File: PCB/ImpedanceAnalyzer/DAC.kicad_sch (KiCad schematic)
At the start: 88 parts, among them U14 OPA4830, U17 OPA4830, U6 LTC1668CG

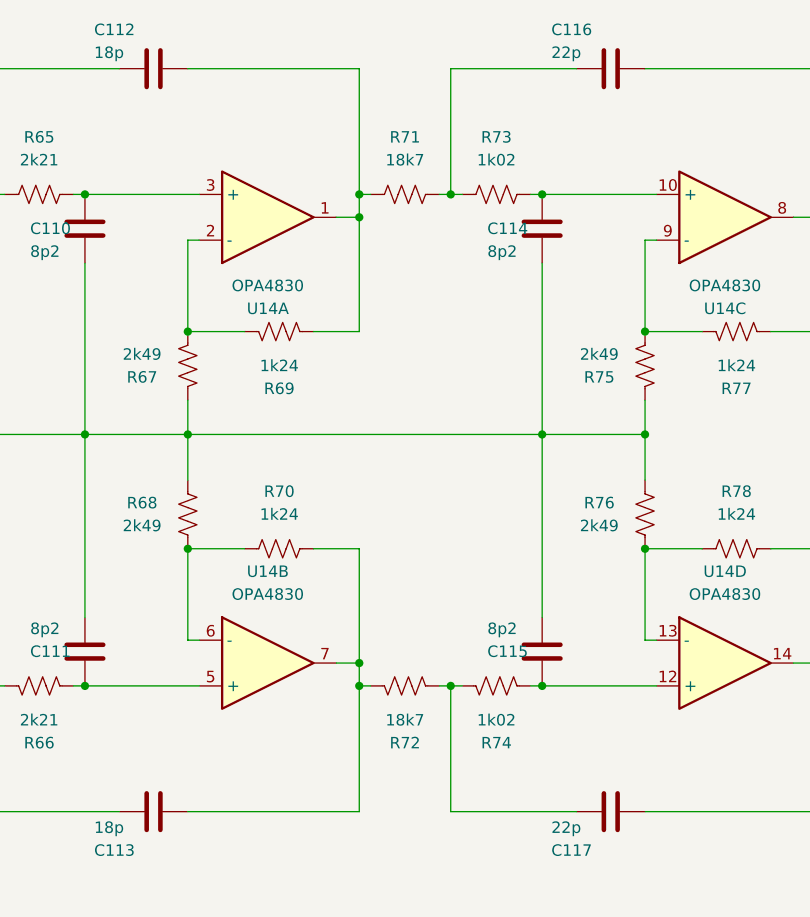
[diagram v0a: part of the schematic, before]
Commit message: STM32 SimpleSample code with PGA and range
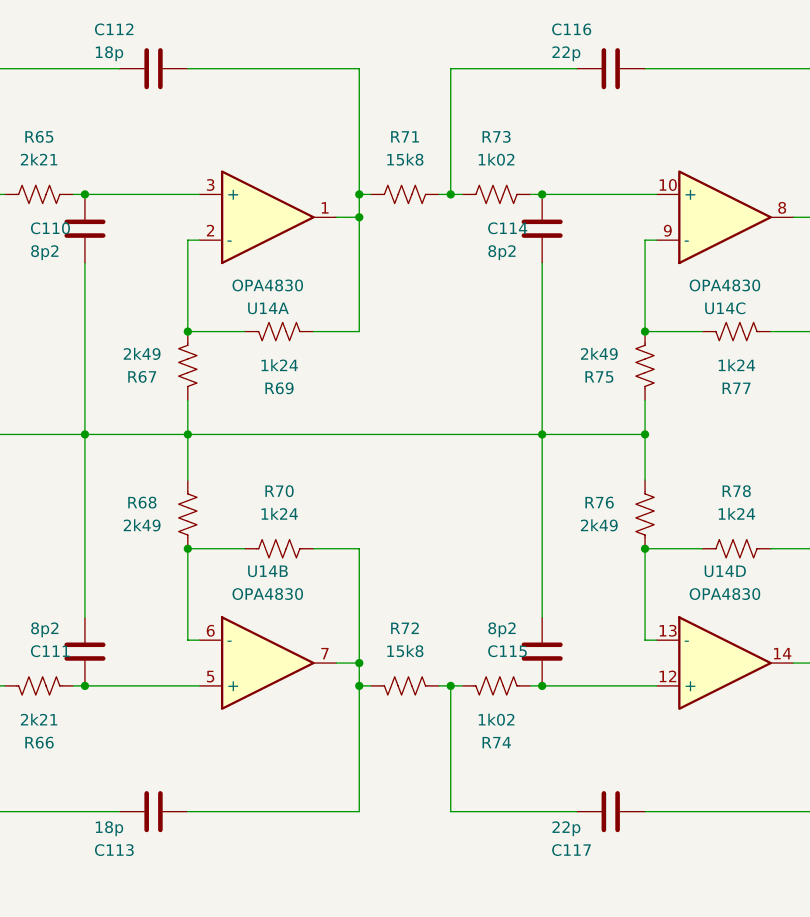
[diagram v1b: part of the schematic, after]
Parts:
- R71, R72: value 18k7 -> 15k8
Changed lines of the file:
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@@
 			)
 		)
-		(property "Value" "18k7"
+		(property "Value" "15k8"
 			(at 345.44 36.83 90)
 			(effects
@@
 		(fields_autoplaced yes)
 		(property "Reference" "R72"
-			(at 345.44 101.6 90)
-			(effects
-				(font
-					(size 1.27 1.27)
-				)
-			)
-		)
-		(property "Value" "18k7"
-			(at 345.44 99.06 90)
-			(effects
-				(font
+			(at 345.44 88.9 90)
+			(effects
+				(font
+					(size 1.27 1.27)
+				)
+			)
+		)
+		(property "Value" "15k8"
+			(at 345.44 91.44 90)
+			(effects
+				(font
